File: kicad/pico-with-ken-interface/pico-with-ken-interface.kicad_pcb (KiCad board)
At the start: 4 copper layers, 81.3 x 81.3 mm, 7 parts, among them U1 Pico, U3 XDZ254-2-15-W-2.5-G1, U5 PM254-2-15-W-8.5

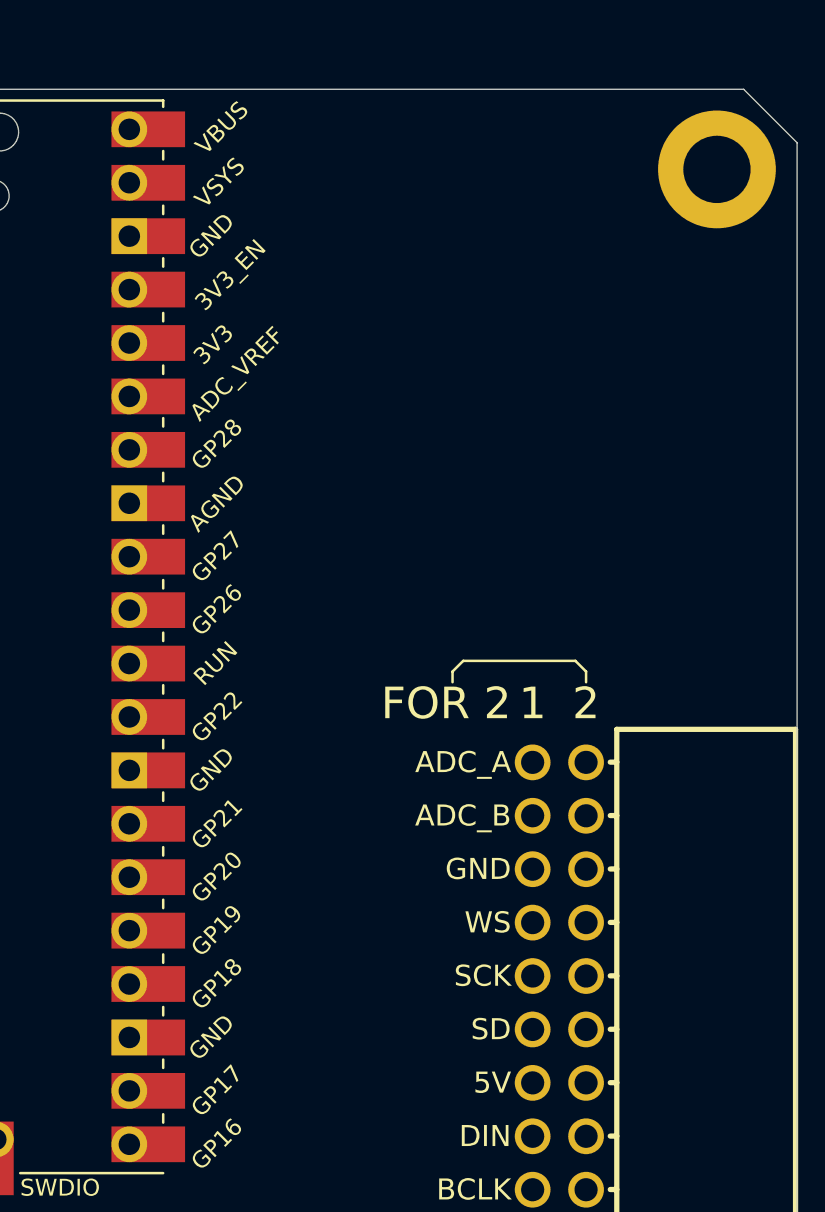
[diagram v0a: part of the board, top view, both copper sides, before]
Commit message: bring back button symbol and foot print, did some routing.
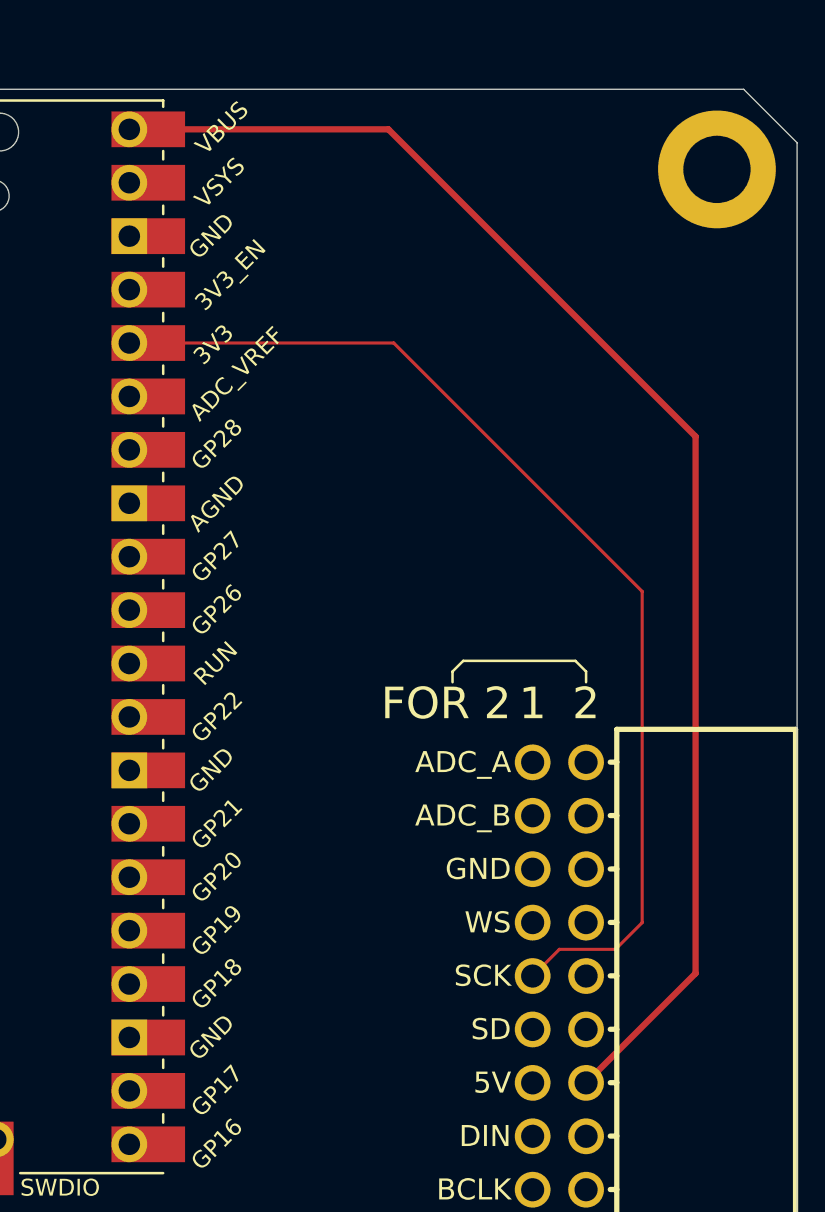
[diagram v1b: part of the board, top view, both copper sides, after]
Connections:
- U1 pad 1: unconnected-(U1-GPIO0-Pad1) -> /GPIO0
- U1 pad 10: unconnected-(U1-GPIO7-Pad10) -> /GPIO7
- U1 pad 11: unconnected-(U1-GPIO8-Pad11) -> /GPIO8
- U1 pad 12: unconnected-(U1-GPIO9-Pad12) -> /GPIO9
- U1 pad 13: unconnected-(U1-GND-Pad13) -> GND
- U1 pad 14: unconnected-(U1-GPIO10-Pad14) -> /GPIO10
- U1 pad 15: unconnected-(U1-GPIO11-Pad15) -> /GPIO11
- U1 pad 16: unconnected-(U1-GPIO12-Pad16) -> /GPIO12
- U1 pad 17: unconnected-(U1-GPIO13-Pad17) -> /GPIO13
- U1 pad 18: unconnected-(U1-GND-Pad18) -> GND
- U1 pad 19: unconnected-(U1-GPIO14-Pad19) -> /GPIO14
- U1 pad 2: unconnected-(U1-GPIO1-Pad2) -> /GPIO1
- U1 pad 20: unconnected-(U1-GPIO15-Pad20) -> /GPIO15
- U1 pad 21: unconnected-(U1-GPIO16-Pad21) -> /GPIO16
- U1 pad 22: unconnected-(U1-GPIO17-Pad22) -> /GPIO17
- U1 pad 23: unconnected-(U1-GND-Pad23) -> GND
- U1 pad 24: unconnected-(U1-GPIO18-Pad24) -> /GPIO18
- U1 pad 25: unconnected-(U1-GPIO19-Pad25) -> /GPIO19
- U1 pad 26: unconnected-(U1-GPIO20-Pad26) -> /GPIO20
- U1 pad 27: unconnected-(U1-GPIO21-Pad27) -> /GPIO21
- U1 pad 28: unconnected-(U1-GND-Pad28) -> GND
- U1 pad 29: unconnected-(U1-GPIO22-Pad29) -> /GPIO22
- U1 pad 3: unconnected-(U1-GND-Pad3) -> GND
- U1 pad 30: unconnected-(U1-RUN-Pad30) -> /RUN
- U1 pad 31: unconnected-(U1-GPIO26_ADC0-Pad31) -> /GPIO26_ADC0
- U1 pad 32: unconnected-(U1-GPIO27_ADC1-Pad32) -> /GPIO27_ADC1
- U1 pad 33: unconnected-(U1-AGND-Pad33) -> GND
- U1 pad 34: unconnected-(U1-GPIO28_ADC2-Pad34) -> /GPIO28_ADC2
- U1 pad 35: unconnected-(U1-ADC_VREF-Pad35) -> /ADC_VREF
- U1 pad 36: unconnected-(U1-3V3-Pad36) -> +3V3
- U1 pad 37: unconnected-(U1-3V3_EN-Pad37) -> /3V3_EN
- U1 pad 38: unconnected-(U1-GND-Pad38) -> GND
- U1 pad 39: unconnected-(U1-VSYS-Pad39) -> /VSYS
- U1 pad 4: unconnected-(U1-GPIO2-Pad4) -> /GPIO2
- U1 pad 40: unconnected-(U1-VBUS-Pad40) -> +5V
- U1 pad 42: unconnected-(U1-GND-Pad42) -> GND
- U1 pad 5: unconnected-(U1-GPIO3-Pad5) -> /GPIO3
- U1 pad 6: unconnected-(U1-GPIO4-Pad6) -> /GPIO4
- U1 pad 7: unconnected-(U1-GPIO5-Pad7) -> /GPIO5
- U1 pad 8: unconnected-(U1-GND-Pad8) -> GND
- U1 pad 9: unconnected-(U1-GPIO6-Pad9) -> /GPIO6
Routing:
- net +5V: track 68.7 -> 151.0 mm
- net /IO17: track 31.1 -> 99.4 mm
- net /IO18: track 31.1 -> 97.8 mm
- net /IO19: track 31.1 -> 96.0 mm
- net /IO20: track 31.1 -> 94.5 mm
- net /I2C_A_SDA: track 31.1 -> 87.9 mm
- net +3V3: track 119.0 -> 175.4 mm
- net /I2C_A_SCL: track 31.1 -> 86.4 mm
- net /ADC_A: track 37.2 -> 91.6 mm
- net /ADC_B: track 37.2 -> 90.6 mm
- net /I2S_A_WS: track 37.2 -> 87.0 mm
- net /I2S_A_SCK: track 37.2 -> 86.4 mm
- net /I2S_A_SD: track 37.2 -> 85.7 mm
- net /I2S_B_BCLK: track 67.9 -> 86.0 mm
- net /IO11: track 61.7 -> 79.4 mm
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
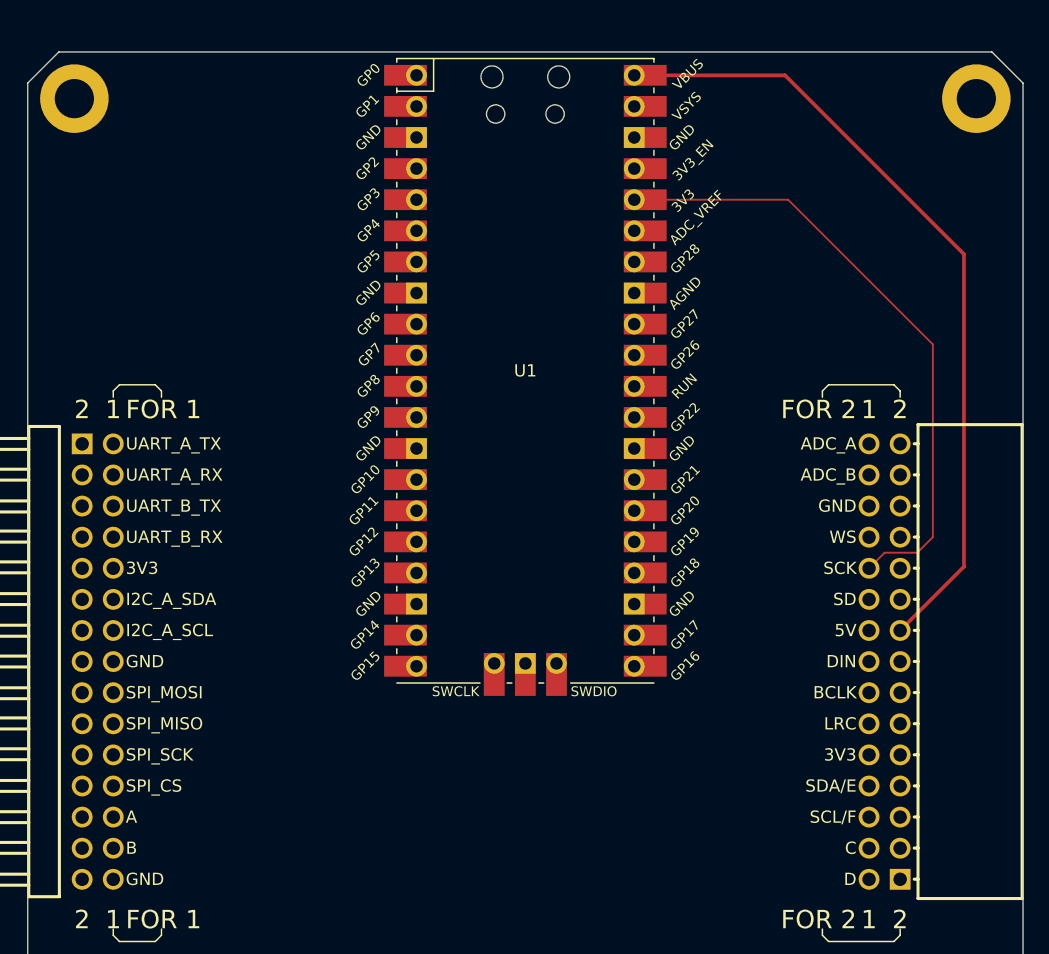
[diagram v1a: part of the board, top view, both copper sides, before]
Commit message: first routing for pico
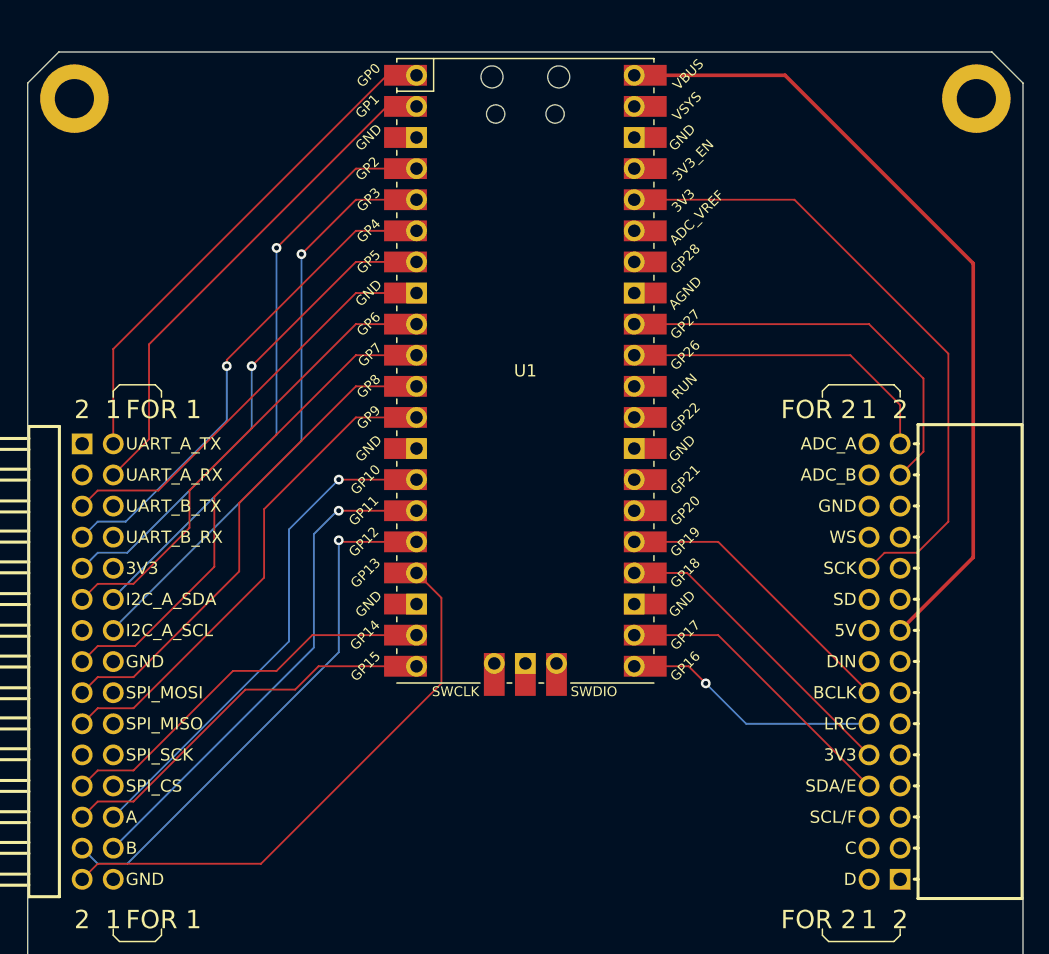
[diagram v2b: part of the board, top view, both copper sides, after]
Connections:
- net /IO19 renamed /UART_B_TX
- net /IO20 renamed /UART_B_RX
- U1 pad 31: /GPIO26_ADC0 -> /ADC_A
- U1 pad 32: /GPIO27_ADC1 -> /ADC_B
- U3 pad 11: /I2S_A_SD -> /GPIO6
- U3 pad 12: /I2C_A_SDA -> /GPIO2
- U3 pad 14: /I2C_A_SCL -> /GPIO3
- U3 pad 15: /I2S_B_DIN -> /GPIO7
- U3 pad 17: /I2S_B_BCLK -> /GPIO8
- U3 pad 18: /IO11 -> /GPIO19
- U3 pad 19: /I2S_B_LRC -> /GPIO9
- U3 pad 2: /IO17 -> /GPIO0
- U3 pad 20: /IO13 -> /GPIO16
- U3 pad 22: /IO12 -> /GPIO18
- U3 pad 23: /I2C_B_SDA -> /GPIO14
- U3 pad 24: /IO10 -> /GPIO17
- U3 pad 25: /I2C_B_SCL -> /GPIO15
- U3 pad 26: /BTN_A -> /GPIO10
- U3 pad 27: /BTN_C -> /GPIO12
- U3 pad 28: /BTN_B -> /GPIO11
- U3 pad 29: /BTN_D -> /GPIO13
- U3 pad 4: /IO18 -> /GPIO1
- U3 pad 7: /I2S_A_WS -> /GPIO4
- U3 pad 9: /I2S_A_SCK -> /GPIO5
- U5 pad 1: /BTN_D -> /GPIO13
- U5 pad 10: /IO12 -> /GPIO18
- U5 pad 11: /I2S_B_LRC -> /GPIO9
- U5 pad 12: /IO13 -> /GPIO16
- U5 pad 13: /I2S_B_BCLK -> /GPIO8
- U5 pad 14: /IO11 -> /GPIO19
- U5 pad 15: /I2S_B_DIN -> /GPIO7
- U5 pad 18: /I2C_A_SCL -> /GPIO3
- U5 pad 19: /I2S_A_SD -> /GPIO6
- U5 pad 20: /I2C_A_SDA -> /GPIO2
- U5 pad 21: /I2S_A_SCK -> /GPIO5
- U5 pad 23: /I2S_A_WS -> /GPIO4
- U5 pad 28: /IO18 -> /GPIO1
- U5 pad 3: /BTN_C -> /GPIO12
- U5 pad 30: /IO17 -> /GPIO0
- U5 pad 4: /BTN_B -> /GPIO11
- U5 pad 5: /I2C_B_SCL -> /GPIO15
- U5 pad 6: /BTN_A -> /GPIO10
- U5 pad 7: /I2C_B_SDA -> /GPIO14
- U5 pad 8: /IO10 -> /GPIO17
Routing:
- net /GPIO0: track 0.00 -> 128.7 mm
- net /GPIO1: track 0.00 -> 127.9 mm
- net /GPIO2: track 0.00 -> 126.9 mm, vias 0 -> 1
- net /GPIO3: track 0.00 -> 126.0 mm, vias 0 -> 1
- net /GPIO4: track 0.00 -> 121.5 mm, vias 0 -> 1
- net /GPIO5: track 0.00 -> 120.7 mm, vias 0 -> 1
- net /GPIO7: track 0.00 -> 118.5 mm
- net /GPIO8: track 0.00 -> 117.6 mm
- net /GPIO6: track 0.00 -> 117.6 mm
- net /GPIO13: track 0.00 -> 117.5 mm
- net /GPIO12: track 0.00 -> 117.3 mm, vias 0 -> 1
- net /GPIO9: track 0.00 -> 116.8 mm
- net /GPIO10: track 0.00 -> 109.8 mm, vias 0 -> 1
- net /GPIO11: track 0.00 -> 109.2 mm, vias 0 -> 1
- net /GPIO14: track 0.00 -> 106.6 mm
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
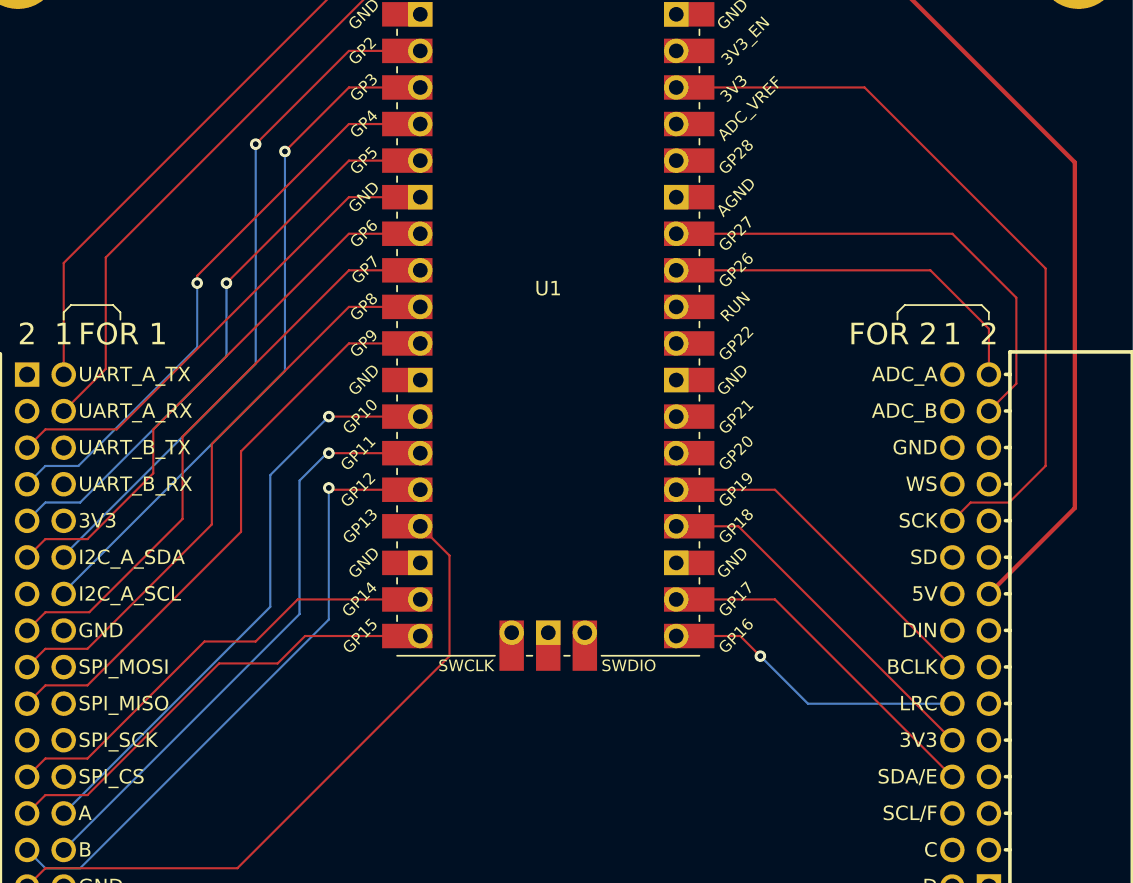
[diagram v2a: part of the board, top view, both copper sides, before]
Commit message: add button and LED
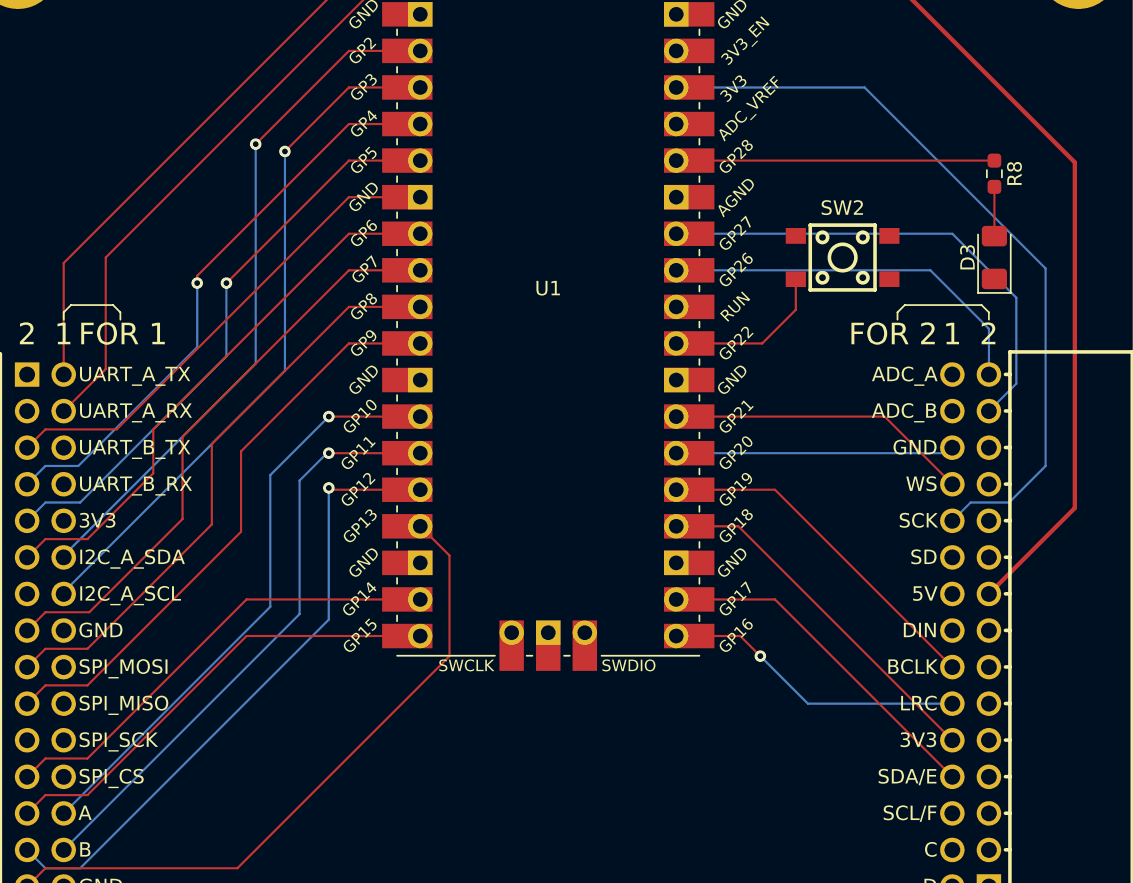
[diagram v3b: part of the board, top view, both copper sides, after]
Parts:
- added D3: LED, LED_SMD:LED_1206_3216Metric_Pad1.42x1.75mm_HandSolder, F.Cu at (130.0, 63.2)
- added R8: 1k, Resistor_SMD:R_0603_1608Metric_Pad0.98x0.95mm_HandSolder, F.Cu at (130.0, 57.4)
- added SW2: TSC015A03526A, TSC015A03526A:SW-SMD_4P-L4.5-W4.5-P3.00-LS6.8, F.Cu at (119.5, 63.2)
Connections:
- U3 pad 6: /UART_B_TX -> /GPIO20
- U3 pad 8: /UART_B_RX -> /GPIO21
- U5 pad 24: /UART_B_RX -> /GPIO21
- U5 pad 26: /UART_B_TX -> /GPIO20
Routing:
- net /GPIO21: track 0.00 -> 105.6 mm
- net /GPIO20: track 0.00 -> 104.6 mm
- net /UART_B_TX: track 85.3 -> 0.00 mm
- net /UART_B_RX: track 84.4 -> 0.00 mm
- net /GPIO28_ADC2: track 0.00 -> 22.1 mm
- net /GPIO22: track 0.00 -> 11.4 mm
- net Net-(D3-A): track 0.00 -> 3.45 mm
